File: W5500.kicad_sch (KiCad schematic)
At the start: 39 parts, among them J6 HR911105A, U4 W5500, Y2 X322525MOB4SI

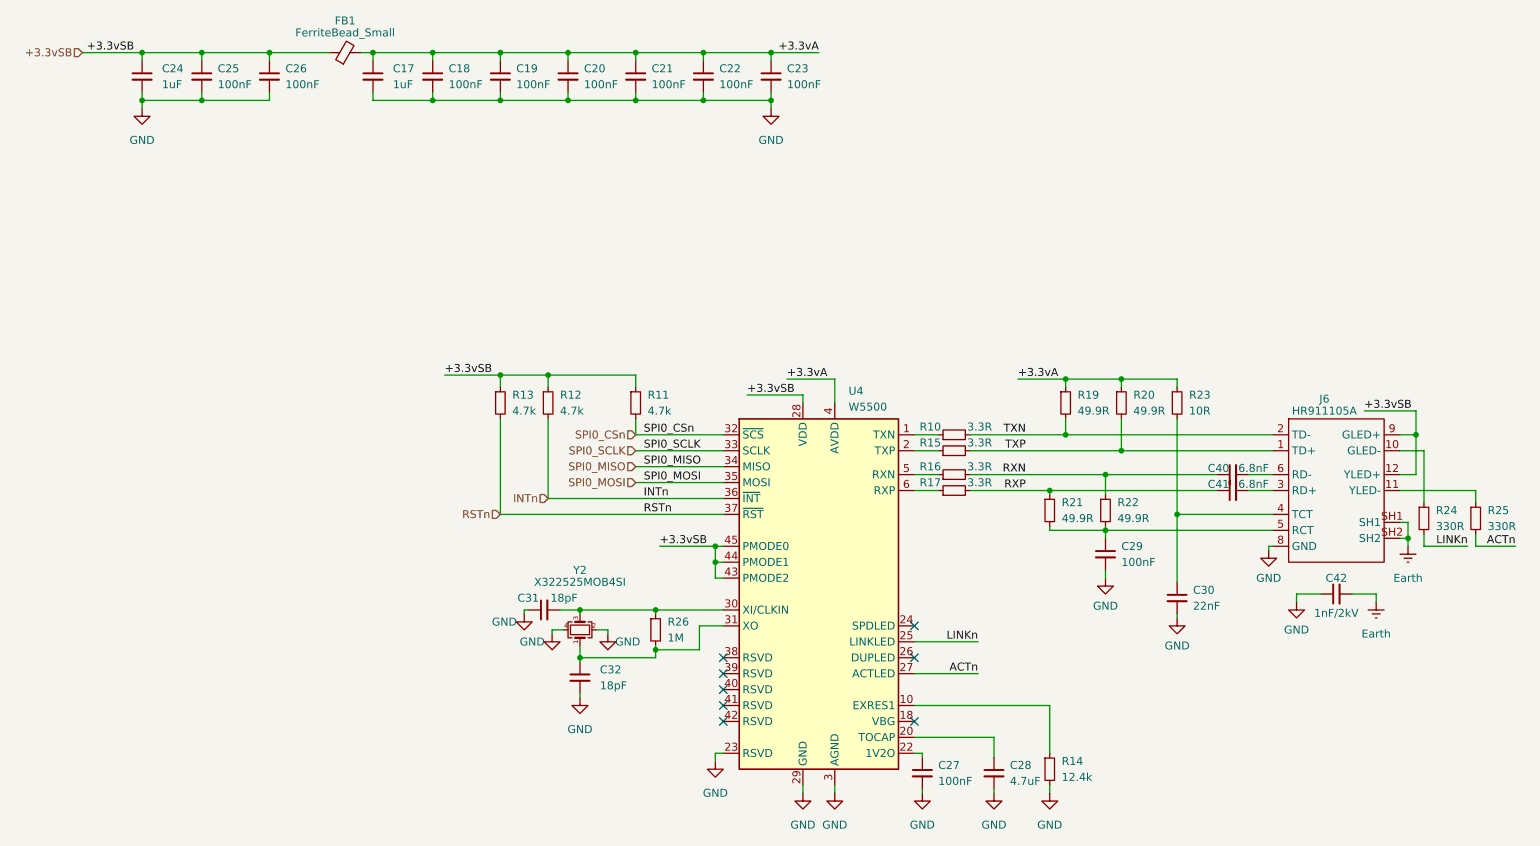
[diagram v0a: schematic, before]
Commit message: Rev4
Bunch of small changes, namely:
Add onboard DS18B20 probe for more accurate temp readings without external hardware.
Rename T1DATA to T2DATA to still allow external probes.
Add USB power sensing circuit.
Add SR latch for PS_ON# handling
Add J4 UART header.
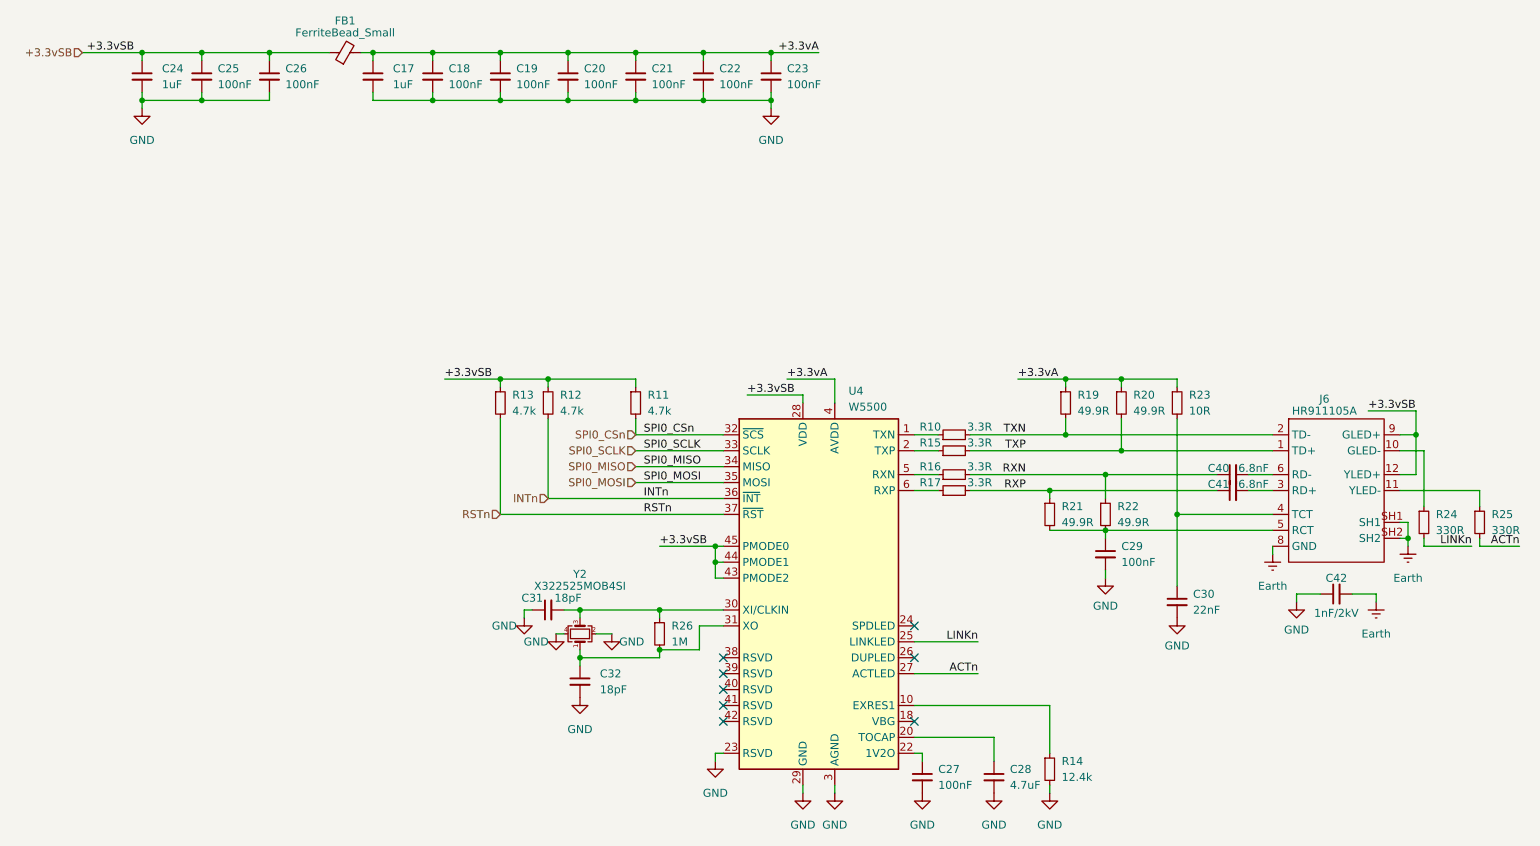
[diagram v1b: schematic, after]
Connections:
- net Earth: now also J6.8 (GND)
- net GND: no longer J6.8 (GND)
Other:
- moved on the sheet: C27, C28, C30, C31, C32, R21, R22, R24, R25, R26, Y2

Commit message: rev5
Added MACROM (specific ROM holding MAC address and (optionally) board
revision)
Added more circuitry to protect the EMC2301, allowing for use with fans
with internal pull-ups.
Added USB-C
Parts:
- C17, C24: JLCPCB_PN C52923 -> (none); LCSC Part # (none) -> C52923
- C18, C19, C20, C21, C22, C23, C25, C26, C27, C29: JLCPCB_PN C1525 -> (none); LCSC Part # (none) -> C1525
- C28: JLCPCB_PN C23733 -> (none); LCSC Part # (none) -> C23733
- C30: JLCPCB_PN C1532 -> (none); LCSC Part # (none) -> C1532
- C31, C32: JLCPCB_PN C1549 -> (none); LCSC Part # (none) -> C1549
- C40, C41: JLCPCB_PN C1542 -> (none); LCSC Part # (none) -> C1542
- C42: JLCPCB_PN C9196 -> (none); LCSC Part # (none) -> C9196
- FB1: JLCPCB_PN C1015 -> (none); LCSC Part # (none) -> C1015
- J6: JLCPCB_PN C12074 -> (none); LCSC Part # (none) -> C12074
- R10, R15, R16, R17: JLCPCB_PN C2930016 -> (none); LCSC Part # (none) -> C2930016
- R11, R12, R13: JLCPCB_PN C25900 -> (none); LCSC Part # (none) -> C25900
- R14: JLCPCB_PN C11692 -> (none); LCSC Part # (none) -> C11692
- R19, R20, R21, R22: JLCPCB_PN C25120 -> (none); LCSC Part # (none) -> C25120
- R23: JLCPCB_PN C25077 -> (none); LCSC Part # (none) -> C25077
- R24, R25: JLCPCB_PN C25104 -> (none); LCSC Part # (none) -> C25104
- R26: JLCPCB_PN C26083 -> (none); LCSC Part # (none) -> C26083
- U4: JLCPCB_PN C32843 -> (none); LCSC Part # (none) -> C32843
- Y2: JLCPCB_PN C9006 -> (none); LCSC Part # (none) -> C9006
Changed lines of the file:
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@@
 (kicad_sch
-	(version 20231120)
+	(version 20250114)
 	(generator "eeschema")
-	(generator_version "8.0")
+	(generator_version "9.0")
 	(paper "A4")
 	(title_block
@@
 	(label "SPI0_MISO"
 		(at 111.76 85.09 0)
-		(fields_autoplaced yes)
 		(effects
 			(font
@@
 	(label "ACTn"
 		(at 165.1 118.11 180)
-		(fields_autoplaced yes)
 		(effects
 			(font
@@
 	(label "+3.3vA"
 		(at 171.45 71.12 0)
-		(fields_autoplaced yes)
 		(effects
 			(font
@@
 	(label "SPI0_MOSI"
 		(at 111.76 87.63 0)
-		(fields_autoplaced yes)
 		(effects
 			(font
@@
 	(label "TXN"
 		(at 172.72 80.01 180)
-		(fields_autoplaced yes)
 		(effects
 			(font
@@
 	(label "INTn"
 		(at 111.76 90.17 0)
-		(fields_autoplaced yes)
 		(effects
 			(font
@@
 	(label "SPI0_SCLK"
 		(at 111.76 82.55 0)
-		(fields_autoplaced yes)
 		(effects
 			(font
@@
 	(label "+3.3vA"
 		(at 134.62 71.12 0)
-		(fields_autoplaced yes)
 		(effects
 			(font
@@
 	(label "RXN"
 		(at 172.72 86.36 180)
-		(fields_autoplaced yes)
 		(effects
 			(font
@@
 	(label "+3.3vSB"
 		(at 30.48 19.05 180)
-		(fields_autoplaced yes)
 		(effects
 			(font
@@
 	(label "+3.3vA"
 		(at 139.7 19.05 180)
-		(fields_autoplaced yes)
 		(effects
 			(font
@@
 	(label "RXP"
 		(at 172.72 88.9 180)
-		(fields_autoplaced yes)
 		(effects
 			(font
@@
 	(label "SPI0_CSn"
 		(at 111.76 80.01 0)
-		(fields_autoplaced yes)
 		(effects
 			(font
@@
 	(label "+3.3vSB"
 		(at 128.27 73.66 0)
-		(fields_autoplaced yes)
 		(effects
 			(font
@@
 	(label "RSTn"
 		(at 111.76 92.71 0)
-		(fields_autoplaced yes)
 		(effects
 			(font
@@
 	(label "+3.3vSB"
 		(at 227.33 76.2 0)
-		(fields_autoplaced yes)
 		(effects
 			(font
@@
 	(label "+3.3vSB"
 		(at 114.3 97.79 0)
-		(fields_autoplaced yes)
 		(effects
 			(font
@@
 	(label "ACTn"
 		(at 251.46 97.79 180)
-		(fields_autoplaced yes)
 		(effects
 			(font
@@
 	(label "TXP"
 		(at 172.72 82.55 180)
-		(fields_autoplaced yes)
 		(effects
 			(font
@@
 	(label "+3.3vSB"
 		(at 80.01 71.12 0)
-		(fields_autoplaced yes)
 		(effects
 			(font
@@
 	(label "LINKn"
 		(at 243.84 97.79 180)
-		(fields_autoplaced yes)
 		(effects
 			(font
@@
 	(label "LINKn"
 		(at 165.1 113.03 180)
-		(fields_autoplaced yes)
 		(effects
 			(font
@@
 		(shape input)
 		(at 22.225 19.05 180)
-		(fields_autoplaced yes)
 		(effects
 			(font
@@
 		(shape input)
 		(at 110.49 85.09 180)
-		(fields_autoplaced yes)
 		(effects
 			(font
@@
 		(shape input)
 		(at 110.49 87.63 180)
-		(fields_autoplaced yes)
 		(effects
 			(font
@@
 		(shape input)
 		(at 88.9 92.71 180)
-		(fields_autoplaced yes)
 		(effects
 			(font
@@
 		(shape input)
 		(at 96.52 90.17 180)
-		(fields_autoplaced yes)
 		(effects
 			(font
@@
 		(shape input)
 		(at 110.49 80.01 180)
-		(fields_autoplaced yes)
 		(effects
 			(font
@@
 		(shape input)
 		(at 110.49 82.55 180)
-		(fields_autoplaced yes)
 		(effects
 			(font
@@
 			)
 		)
-		(property "JLCPCB_PN" "C52923"
+		(property "LCSC Part #" "C52923"
 			(at 31.75 22.86 0)
 			(effects
@@
 			)
 		)
-		(property "JLCPCB_PN" "C25077"
+		(property "LCSC Part #" "C25077"
 			(at 196.85 74.93 0)
 			(effects
@@
 			)
 		)
-		(property "JLCPCB_PN" "C1525"
+		(property "LCSC Part #" "C1525"
 			(at 121.285 22.86 0)
 			(effects
@@
 			)
 		)
-		(property "JLCPCB_PN" "C1525"
+		(property "LCSC Part #" "C1525"
 			(at 132.08 22.86 0)
 			(effects
@@
 			)
 		)
-		(property "JLCPCB_PN" "C25900"
+		(property "LCSC Part #" "C25900"
 			(at 96.52 74.93 0)
 			(effects
@@
 			)
 		)
-		(property "JLCPCB_PN" "C52923"
+		(property "LCSC Part #" "C52923"
 			(at 68.58 22.86 0)
 			(effects
@@
 			)
 		)
-		(property "JLCPCB_PN" "C26083"
+		(property "LCSC Part #" "C26083"
 			(at 114.3 111.76 0)
 			(effects
@@
 			)
 		)
-		(property "JLCPCB_PN" "C1542"
-			(at 205.74 86.36 90)
+		(property "LCSC Part #" "C1542"
+			(at 205.74 86.36 0)
 			(effects
 				(font
@@
 			)
 		)
-		(property "JLCPCB_PN" "C1525"
+		(property "LCSC Part #" "C1525"
 			(at 78.105 22.86 0)
 			(effects
@@
 			)
 		)
-		(property "JLCPCB_PN" "C25120"
+		(property "LCSC Part #" "C25120"
 			(at 187.96 74.93 0)
 			(effects
@@
 			)
 		)
-		(property "JLCPCB_PN" "C25120"
+		(property "LCSC Part #" "C25120"
 			(at 176.53 92.71 0)
 			(effects
@@
 			)
 		)
-		(property "JLCPCB_PN" "C25104"
+		(property "LCSC Part #" "C25104"
 			(at 245.11 93.98 0)
 			(effects
@@
 			)
 		)
-		(property "JLCPCB_PN" "C12074"
+		(property "LCSC Part #" "C12074"
 			(at 212.09 77.47 0)
 			(effects
@@
 			)
 		)
-		(property "JLCPCB_PN" "C2930016"
+		(property "LCSC Part #" "C2930016"
 			(at 161.29 88.9 0)
 			(effects
@@
 			)
 		)
-		(property "JLCPCB_PN" "C25120"
+		(property "LCSC Part #" "C25120"
 			(at 185.42 92.71 0)
 			(effects
@@
 			)
 		)
-		(property "JLCPCB_PN" "C1525"
+		(property "LCSC Part #" "C1525"
 			(at 41.275 22.86 0)
 			(effects
@@
 			)
 		)
-		(property "JLCPCB_PN" "C25104"
+		(property "LCSC Part #" "C25104"
 			(at 236.22 93.98 0)
 			(effects
@@
 			)
 		)
-		(property "JLCPCB_PN" "C2930016"
+		(property "LCSC Part #" "C2930016"
 			(at 161.29 86.36 0)
 			(effects
@@
 			)
 		)
-		(property "JLCPCB_PN" "C11692"
+		(property "LCSC Part #" "C11692"
 			(at 176.53 133.35 0)
 			(effects
@@
 			)
 		)
-		(property "JLCPCB_PN" "C1549"
+		(property "LCSC Part #" "C1549"
 			(at 96.52 107.95 0)
 			(effects
@@
 			)
 		)
-		(property "JLCPCB_PN" "C25120"
+		(property "LCSC Part #" "C25120"
 			(at 179.07 74.93 0)
 			(effects
@@
 			)
 		)
-		(property "JLCPCB_PN" "C1525"
+		(property "LCSC Part #" "C1525"
 			(at 156.21 134.62 0)
 			(effects
@@
 			)
 		)
-		(property "JLCPCB_PN" "C9196"
-			(at 222.25 105.41 90)
+		(property "LCSC Part #" "C9196"
+			(at 222.25 105.41 0)
 			(effects
 				(font
@@
 			)
 		)
-		(property "JLCPCB_PN" "C25900"
+		(property "LCSC Part #" "C25900"
 			(at 110.49 74.93 0)
 			(effects
@@
 			)
 		)
-		(property "JLCPCB_PN" "C1525"
+		(property "LCSC Part #" "C1525"
 			(at 99.695 22.86 0)
 			(effects
@@
 			)
 		)
-		(property "JLCPCB_PN" "C2930016"
+		(property "LCSC Part #" "C2930016"
 			(at 161.29 80.01 0)
 			(effects
@@
 			)
 		)
-		(property "JLCPCB_PN" "C1525"
+		(property "LCSC Part #" "C1525"
 			(at 52.07 22.86 0)
 			(effects
@@
 			)
 		)
-		(property "JLCPCB_PN" "C1015"
+		(property "LCSC Part #" "C1015"
 			(at 64.135 19.05 0)
 			(effects
@@
 			)
 		)
-		(property "JLCPCB_PN" "C9006"
+		(property "LCSC Part #" "C9006"
 			(at 101.6 111.76 0)
 			(effects
@@
 			)
 		)
-		(property "JLCPCB_PN" "C1525"
+		(property "LCSC Part #" "C1525"
 			(at 185.42 99.06 0)
 			(effects
@@
 			)
 		)
-		(property "JLCPCB_PN" "C1525"
+		(property "LCSC Part #" "C1525"
 			(at 88.9 22.86 0)
 			(effects
@@
 			)
 		)
-		(property "JLCPCB_PN" "C25900"
+		(property "LCSC Part #" "C25900"
 			(at 88.9 74.93 0)
 			(effects
@@
 			)
 		)
-		(property "JLCPCB_PN" "C23733"
+		(property "LCSC Part #" "C23733"
 			(at 167.64 134.62 0)
 			(effects
@@
 			)
 		)
-		(property "JLCPCB_PN" "C1532"
+		(property "LCSC Part #" "C1532"
 			(at 196.85 106.68 0)
 			(effects
@@
 			)
 		)
-		(property "JLCPCB_PN" "C1542"
-			(at 205.74 88.9 90)
+		(property "LCSC Part #" "C1542"
+			(at 205.74 88.9 0)
 			(effects
 				(font
@@
 			)
 		)
-		(property "JLCPCB_PN" "C1525"
+		(property "LCSC Part #" "C1525"
 			(at 110.49 22.86 0)
 			(effects
@@
 			)
 		)
-		(property "JLCPCB_PN" "C1549"
+		(property "LCSC Part #" "C1549"
 			(at 101.6 119.38 0)
 			(effects
@@
 			)
 		)
-		(property "JLCPCB_PN" "C2930016"
+		(property "LCSC Part #" "C2930016"
 			(at 161.29 82.55 0)
 			(effects
@@
 			)
 		)
-		(property "JLCPCB_PN" "C32843"
+		(property "LCSC Part #" "C32843"
 			(at 139.7 105.41 0)
 			(effects
